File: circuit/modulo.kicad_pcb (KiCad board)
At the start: 2 copper layers, 302 x 135 mm, 201 parts, among them J1 JACK_MONO, J10 HOLE, J11 HOLE, J12 HOLE, J13 HOLE, J14 HOLE, J15 HOLE, J17 HOLE, J18 HOLE, J19 HOLE, J2 Barrel_Jack_Switch, J24 HOLE, J25 HOLE, J26 HOLE, J27 HOLE, J3 HOLE, J4 HOLE, J5 HOLE, J6 HOLE, J7 HOLE, J8 HOLE, J9 HOLE, Q1 MMBFJ201, Q2 BC547, Q3 BC557, Q4 BC547, Q5 BC557, SW1 OFF/ON, SW2 ROT_SW, SW3 Idss/Vp, SW4 disc/TLE2426, SW5 disc/TLE2426, U1 TLE2426, U10 AVR-ISP6, U11 74164, U12 TPA3136D2, U13 74164, U14 modulo-bus, U15 modulo-bus, U16 modulo-bus, U17 TLE2426, U18 DBG_UART, U19 TPS560430, U2 NE5532, U3 FV-1, U4 NE5532, U5 24LC32A, U6 modulo-bus, U7 LM1117, U8 modulo-bus, U9 ATMEGA8, Y1 32768Hz, Y2 8MHz

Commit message: added pot and rotenc datasheets; cosmetics
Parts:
- moved J1 0.32 mm to (11.7, 17.8)
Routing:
- net +12V: track 508.1 -> 503.5 mm
- net Net-(RV6-Pad2): track 55.2 -> 54.1 mm
- net /pre amp/jfet_g: track 49.4 -> 50.1 mm

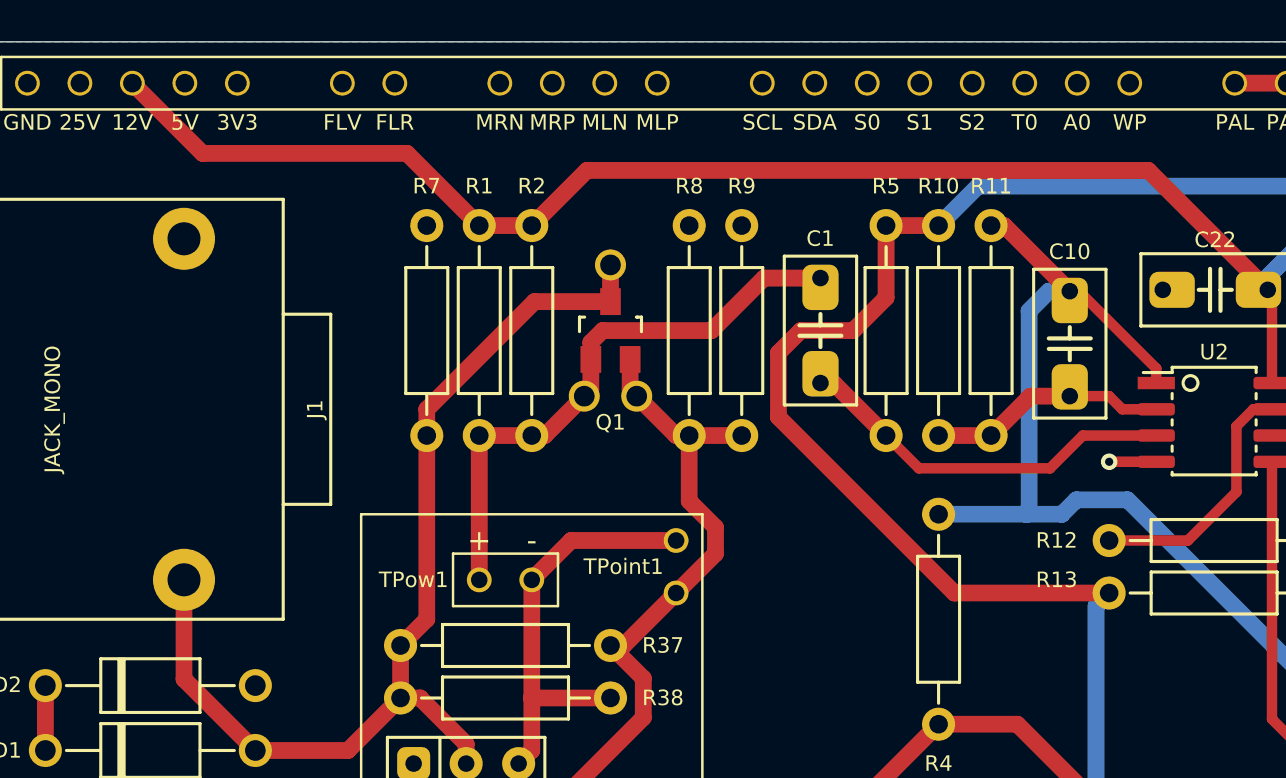
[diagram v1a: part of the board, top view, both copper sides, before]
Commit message: ccw/cw on pots; new values of the tone stack
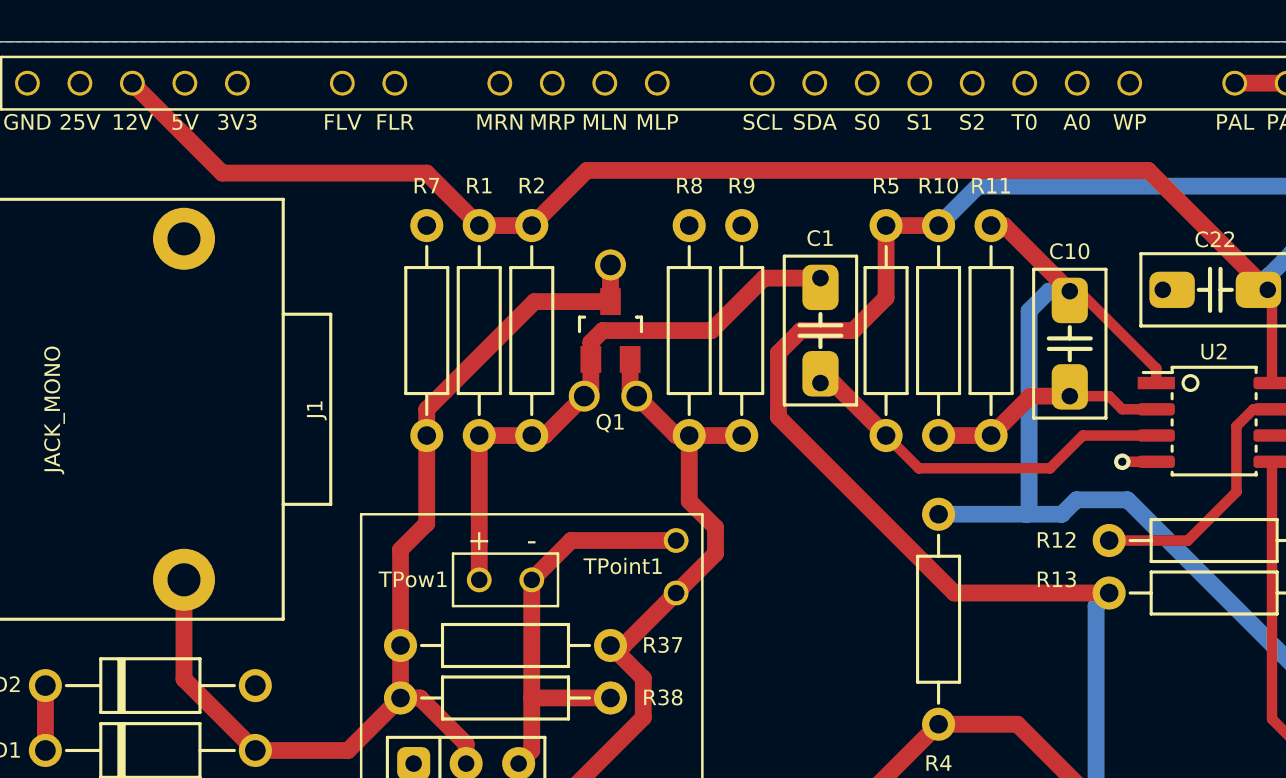
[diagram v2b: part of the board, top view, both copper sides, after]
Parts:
- C2: value 250pF -> 680pF
- C8: value 100nF -> 250nF
- RV1, RV2: value 250K -> A100K
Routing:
- net GND: track 108.9 -> 108.3 mm
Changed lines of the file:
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@@
     (thickness 1.6)
     (drawings 50)
-    (tracks 1037)
+    (tracks 1038)
     (zones 0)
     (modules 201)
@@
   )
   (setup
-    (last_trace_width 0.8128)
+    (last_trace_width 0.2032)
     (user_trace_width 0.254)
     (user_trace_width 0.3048)
@@
       (effects (font (size 0.75 0.75) (thickness 0.15)))
     )
-    (fp_text value 100nF (at -1.016 -0.254) (layer F.Fab) hide
+    (fp_text value 250nF (at -1.016 -0.254) (layer F.Fab) hide
       (effects (font (size 0.127 0.127) (thickness 0.001)))
     )
@@
       (effects (font (size 0.75 0.75) (thickness 0.15)))
     )
-    (fp_text value 250pF (at -1.016 -0.254) (layer F.Fab) hide
+    (fp_text value 680pF (at -1.016 -0.254) (layer F.Fab) hide
       (effects (font (size 0.127 0.127) (thickness 0.001)))
     )
@@
       (effects (font (size 0.75 0.75) (thickness 0.15)))
     )
-    (fp_text value 250K (at 0 -0.5) (layer F.Fab)
+    (fp_text value A100K (at 0 -0.5) (layer F.Fab)
       (effects (font (size 0.03 0.03) (thickness 0.0075)))
     )
@@
       (effects (font (size 0.75 0.75) (thickness 0.15)))
     )
-    (fp_text value 250K (at 0 -0.5) (layer F.Fab)
+    (fp_text value A100K (at 0 -0.5) (layer F.Fab)
       (effects (font (size 0.03 0.03) (thickness 0.0075)))
     )
@@
   (via (at 38.735 105.41) (size 0.8) (drill 0.4) (layers F.Cu B.Cu) (net 3))
   (segment (start 40.38 105.41) (end 38.735 105.41) (width 0.508) (layer F.Cu) (net 3))
-  (via (at 62.865 20.32) (size 0.8) (drill 0.4) (layers F.Cu B.Cu) (net 3))
-  (segment (start 65.145 20.32) (end 62.865 20.32) (width 0.508) (layer F.Cu) (net 3))
+  (segment (start 65.145 20.32) (end 63.5 20.32) (width 0.508) (layer F.Cu) (net 3))
+  (via (at 63.5 20.32) (size 0.8) (drill 0.4) (layers F.Cu B.Cu) (net 3))
   (segment (start 257.445 24.765) (end 257.6 24.61) (width 0.508) (layer F.Cu) (net 4))
   (segment (start 253.085 24.765) (end 257.445 24.765) (width 0.508) (layer F.Cu) (net 4))
@@
   (segment (start 70.54 11.37) (end 71.75 10.16) (width 0.8128) (layer B.Cu) (net 57))
   (segment (start 32.385 8.89) (end 34.925 8.89) (width 0.8128) (layer F.Cu) (net 57))
-  (segment (start 15.6 2) (end 18.9975 5.3975) (width 0.8128) (layer F.Cu) (net 57))
-  (segment (start 28.8925 5.3975) (end 32.385 8.89) (width 0.8128) (layer F.Cu) (net 57))
-  (segment (start 18.9975 5.3975) (end 28.8925 5.3975) (width 0.8128) (layer F.Cu) (net 57))
   (segment (start 34.925 8.89) (end 37.592 6.223) (width 0.8128) (layer F.Cu) (net 57))
   (segment (start 64.763 6.223) (end 70.54 12) (width 0.8128) (layer F.Cu) (net 57))
@@
   (segment (start 120.65 38.0365) (end 120.65 27.94) (width 0.8128) (layer F.Cu) (net 57))
   (segment (start 119.22125 39.46525) (end 120.65 38.0365) (width 0.8128) (layer F.Cu) (net 57))
+  (segment (start 29.845 6.35) (end 32.385 8.89) (width 0.8128) (layer F.Cu) (net 57))
+  (segment (start 15.6 2) (end 19.95 6.35) (width 0.8128) (layer F.Cu) (net 57))
+  (segment (start 19.95 6.35) (end 29.845 6.35) (width 0.8128) (layer F.Cu) (net 57))
   (segment (start 65.145 16.51) (end 65.145 15.8055) (width 0.508) (layer F.Cu) (net 58))
   (segment (start 61.4045 12.065) (end 60.96 12.065) (width 0.508) (layer F.Cu) (net 58))
@@
   (segment (start 38.735 12.57) (end 35.055 12.57) (width 0.8128) (layer F.Cu) (net 60))
   (segment (start 35.055 12.57) (end 29.845 17.78) (width 0.8128) (layer F.Cu) (net 60))
-  (segment (start 29.845 27.94) (end 28.575 29.21) (width 0.8128) (layer F.Cu) (net 60))
-  (segment (start 29.845 19.05) (end 29.845 27.94) (width 0.8128) (layer F.Cu) (net 60))
   (segment (start 28.575 29.21) (end 28.575 31.75) (width 0.8128) (layer F.Cu) (net 60))
   (segment (start 26.035 34.29) (end 28.575 31.75) (width 0.8128) (layer F.Cu) (net 60))
@@
   (segment (start 18.0975 30.837501) (end 21.549999 34.29) (width 0.8128) (layer F.Cu) (net 60))
   (segment (start 18.0975 26.03) (end 18.0975 30.837501) (width 0.8128) (layer F.Cu) (net 60))
+  (segment (start 28.575 24.5745) (end 28.575 29.21) (width 0.8128) (layer F.Cu) (net 60))
+  (segment (start 29.845 19.05) (end 29.845 23.3045) (width 0.8128) (layer F.Cu) (net 60))
+  (segment (start 29.845 23.3045) (end 28.575 24.5745) (width 0.8128) (layer F.Cu) (net 60))
   (segment (start 37.785 16.825) (end 37.465 17.145) (width 0.8128) (layer F.Cu) (net 61))
   (segment (start 37.785 15.37) (end 37.785 16.825) (width 0.8128) (layer F.Cu) (net 61))

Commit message: front copper plant; pot descriptions
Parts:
- moved C12 5.43 mm to (48.9, 34.3), turned to 180 degrees
- moved C2 5.08 mm to (74.9, 34.3)
- moved C8 5.08 mm to (62.2, 34.3)
- moved Q2 5.08 mm to (94.6, 33.0)
- moved Q3 5.08 mm to (87.0, 33.0)
- moved D4 4.45 mm to (94.6, 24.8)
- moved D5 4.45 mm to (87.0, 24.8)
- moved R15 4.45 mm to (97.2, 24.8)
- moved R22 4.45 mm to (92.1, 24.8)
- moved R25 4.45 mm to (89.5, 24.8)
- moved R27 4.45 mm to (84.5, 24.8)
- moved C16 3.17 mm to (94.6, 14.0)
- moved C20 3.17 mm to (87.0, 14.0)
- moved U1 1.27 mm to (90.8, 8.26)
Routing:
- net Net-(C12-Pad1): track 21.8 -> 15.0 mm
- net Net-(C12-Pad2): track 55.6 -> 50.2 mm
- net Net-(C8-Pad1): track 52.5 -> 57.6 mm
- net Net-(C10-Pad1): track 54.0 -> 49.0 mm
- net /pre amp/vgnd_disc: track 36.8 -> 32.4 mm
- net +12V: track 503.5 -> 499.7 mm
- net /power and MCU/SCL: track 21.0 -> 23.2 mm
- net Net-(C2-Pad1): track 13.5 -> 15.6 mm
- net Net-(RN2-Pad7): track 26.9 -> 28.6 mm
- net /power and MCU/SDA: track 20.3 -> 21.7 mm
- net /pre amp/vgnd_tle: track 6.35 -> 5.08 mm
- net Net-(C31-Pad1): track 21.9 -> 22.6 mm
- net Net-(Q3-Pad3): track 3.81 -> 3.18 mm
- net Net-(Q2-Pad3): track 3.81 -> 3.18 mm
- net Net-(D5-Pad1): track 7.62 -> 6.99 mm
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- added copper zone on F.Cu, net GND
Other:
- board text added: "bass"
- board text added: "master"
- board text added: "mid"
- board text added: "param 1"
- board text added: "param 2"
- board text added: "param 3"
- board text added: "program"
- board text added: "treble"
- board text added: "wet/dry"

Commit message: this one goes to fab
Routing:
- net +3V3: track 334.3 -> 339.7 mm
- net Net-(RV1-Pad2): track 35.2 -> 32.0 mm
- net Net-(C8-Pad1): track 57.6 -> 58.1 mm
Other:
- board text added: "2020/jun/21"
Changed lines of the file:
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@@
   (general
     (thickness 1.6)
-    (drawings 59)
-    (tracks 1072)
+    (drawings 64)
+    (tracks 1071)
     (zones 0)
     (modules 201)
@@
   )
   (setup
-    (last_trace_width 0.4064)
+    (last_trace_width 0.2032)
     (user_trace_width 0.254)
     (user_trace_width 0.3048)
@@
     )
   )
+  (gr_text 2020/jun/21 (at 179.5145 116.3955) (layer B.SilkS)
+    (effects (font (size 2 2) (thickness 0.4)) (justify mirror))
+  )
+  (gr_text 2020/jun/21 (at 289.56 36.449) (layer B.SilkS)
+    (effects (font (size 2 2) (thickness 0.4)) (justify mirror))
+  )
+  (gr_text 2020/jun/21 (at 85.0265 96.4565) (layer B.SilkS)
+    (effects (font (size 2 2) (thickness 0.4)) (justify mirror))
+  )
+  (gr_text 2020/jun/21 (at 172.6565 7.747) (layer B.SilkS)
+    (effects (font (size 2 2) (thickness 0.4)) (justify mirror))
+  )
+  (gr_text 2020/jun/21 (at 15.113 15.8115) (layer B.SilkS)
+    (effects (font (size 2 2) (thickness 0.4)) (justify mirror))
+  )
   (gr_text "param 3" (at 285.115 41.91) (layer F.SilkS)
     (effects (font (size 2 2) (thickness 0.3)))
@@
   (segment (start 51.435 34.29) (end 53.34 34.29) (width 0.8128) (layer F.Cu) (net 6))
   (segment (start 35.56 44.45) (end 38.06 44.45) (width 0.8128) (layer F.Cu) (net 7))
-  (segment (start 38.5045 44.0055) (end 38.06 44.45) (width 0.8128) (layer F.Cu) (net 7))
-  (segment (start 52.54625 44.0055) (end 38.5045 44.0055) (width 0.8128) (layer F.Cu) (net 7))
-  (segment (start 59.69 39.37) (end 57.18175 39.37) (width 0.8128) (layer F.Cu) (net 7))
-  (segment (start 57.18175 39.37) (end 52.54625 44.0055) (width 0.8128) (layer F.Cu) (net 7))
   (segment (start 59.69 39.37) (end 61.595 39.37) (width 0.8128) (layer F.Cu) (net 7))
   (segment (start 66.675 44.45) (end 83.86 44.45) (width 0.8128) (layer F.Cu) (net 7))
   (segment (start 61.595 39.37) (end 66.675 44.45) (width 0.8128) (layer F.Cu) (net 7))
   (segment (start 59.69 34.29) (end 59.69 39.37) (width 0.8128) (layer F.Cu) (net 7))
+  (segment (start 55.499 44.45) (end 38.06 44.45) (width 0.8128) (layer F.Cu) (net 7))
+  (segment (start 59.69 39.37) (end 59.69 40.259) (width 0.8128) (layer F.Cu) (net 7))
+  (segment (start 59.69 40.259) (end 55.499 44.45) (width 0.8128) (layer F.Cu) (net 7))
   (segment (start 54.61 19.05) (end 57.15 19.05) (width 0.8128) (layer F.Cu) (net 8))
   (segment (start 59.055 17.145) (end 57.15 19.05) (width 0.8128) (layer F.Cu) (net 8))
@@
   (segment (start 251.2695 28.575) (end 253.085 28.575) (width 0.508) (layer F.Cu) (net 10))
   (segment (start 250.15 29.6945) (end 251.2695 28.575) (width 0.508) (layer F.Cu) (net 10))
-  (segment (start 224.75 43.394) (end 224.75 44.45) (width 0.8128) (layer F.Cu) (net 10))
-  (segment (start 216.916 35.56) (end 224.75 43.394) (width 0.8128) (layer F.Cu) (net 10))
-  (segment (start 228.715 28.575) (end 228.715 29.282106) (width 0.8128) (layer F.Cu) (net 10))
-  (segment (start 226.183606 31.8135) (end 218.2495 31.8135) (width 0.8128) (layer F.Cu) (net 10))
-  (segment (start 218.2495 31.8135) (end 216.916 33.147) (width 0.8128) (layer F.Cu) (net 10))
-  (segment (start 216.916 33.147) (end 216.916 35.56) (width 0.8128) (layer F.Cu) (net 10))
-  (segment (start 229.87 33.655) (end 227.137803 30.922803) (width 0.8128) (layer F.Cu) (net 10))
-  (segment (start 228.715 29.282106) (end 227.137803 30.859303) (width 0.8128) (layer F.Cu) (net 10))
-  (segment (start 227.137803 30.922803) (end 227.137803 30.859303) (width 0.8128) (layer F.Cu) (net 10))
-  (segment (start 227.137803 30.859303) (end 226.183606 31.8135) (width 0.8128) (layer F.Cu) (net 10))
   (segment (start 283.7415 44.45) (end 286.266 46.9745) (width 0.8128) (layer F.Cu) (net 10))
   (segment (start 275.55 44.45) (end 283.7415 44.45) (width 0.8128) (layer F.Cu) (net 10))
@@
   (segment (start 175.475889 115.531889) (end 172.2755 112.3315) (width 0.4064) (layer F.Cu) (net 10))
   (segment (start 172.2755 112.3315) (end 165.227 112.3315) (width 0.4064) (layer F.Cu) (net 10))
+  (segment (start 228.715 32.5) (end 229.87 33.655) (width 0.8128) (layer F.Cu) (net 10))
+  (segment (start 228.715 30.214) (end 228.715 32.5) (width 0.8128) (layer F.Cu) (net 10))
+  (segment (start 228.715 28.575) (end 228.715 30.214) (width 0.8128) (layer F.Cu) (net 10))
+  (segment (start 224.75 43.3305) (end 224.75 44.45) (width 0.8128) (layer F.Cu) (net 10))
+  (segment (start 222.0595 40.64) (end 224.75 43.3305) (width 0.8128) (layer F.Cu) (net 10))
+  (segment (start 217.3725 30.214) (end 215.265 32.3215) (width 0.8128) (layer F.Cu) (net 10))
+  (segment (start 228.715 30.214) (end 217.3725 30.214) (width 0.8128) (layer F.Cu) (net 10))
+  (segment (start 215.265 32.3215) (end 215.265 37.4015) (width 0.8128) (layer F.Cu) (net 10))
+  (segment (start 215.265 37.4015) (end 218.5035 40.64) (width 0.8128) (layer F.Cu) (net 10))
+  (segment (start 218.5035 40.64) (end 222.0595 40.64) (width 0.8128) (layer F.Cu) (net 10))
   (segment (start 27.94 100.33) (end 27.94 102.87) (width 0.8128) (layer F.Cu) (net 11))
   (segment (start 64.77 99.06) (end 64.77 101.6) (width 0.8128) (layer F.Cu) (net 12))
@@
   (segment (start 253.085 23.495) (end 255.215 23.495) (width 0.508) (layer F.Cu) (net 53))
   (segment (start 86.36 44.069) (end 86.36 44.45) (width 0.508) (layer F.Cu) (net 54))
-  (segment (start 84.963 42.672) (end 86.36 44.069) (width 0.508) (layer F.Cu) (net 54))
   (segment (start 70.745 28.2) (end 74.93 32.385) (width 0.508) (layer F.Cu) (net 54))
-  (segment (start 74.93 32.385) (end 74.93 40.5765) (width 0.508) (layer F.Cu) (net 54))
   (segment (start 70.745 20.32) (end 70.745 28.2) (width 0.508) (layer F.Cu) (net 54))
-  (segment (start 74.93 40.5765) (end 77.0255 42.672) (width 0.508) (layer F.Cu) (net 54))
-  (segment (start 77.0255 42.672) (end 84.963 42.672) (width 0.508) (layer F.Cu) (net 54))
+  (segment (start 74.93 32.385) (end 74.93 35.1155) (width 0.508) (layer F.Cu) (net 54))
+  (segment (start 74.93 35.1155) (end 75.946 36.1315) (width 0.508) (layer F.Cu) (net 54))
+  (segment (start 78.4225 36.1315) (end 86.36 44.069) (width 0.508) (layer F.Cu) (net 54))
+  (segment (start 75.946 36.1315) (end 78.4225 36.1315) (width 0.508) (layer F.Cu) (net 54))
   (segment (start 273.05 45.4025) (end 273.05 44.45) (width 0.508) (layer F.Cu) (net 55))
   (segment (start 271.2085 47.244) (end 273.05 45.4025) (width 0.508) (layer F.Cu) (net 55))
@@
   (segment (start 251.523496 18.415) (end 249.809 16.700504) (width 0.508) (layer F.Cu) (net 94))
   (segment (start 253.085 18.415) (end 251.523496 18.415) (width 0.508) (layer F.Cu) (net 94))
-  (segment (start 246.4435 13.335004) (end 249.809 16.700504) (width 0.8128) (layer B.Cu) (net 94))
-  (segment (start 246.4435 11.3665) (end 246.4435 13.335004) (width 0.8128) (layer B.Cu) (net 94))
+  (segment (start 247.5865 12.5095) (end 247.5865 14.478004) (width 0.8128) (layer B.Cu) (net 94))
   (segment (start 244.475 10.16) (end 245.237 10.16) (width 0.8128) (layer B.Cu) (net 94))
-  (segment (start 245.237 10.16) (end 246.4435 11.3665) (width 0.8128) (layer B.Cu) (net 94))
+  (segment (start 247.5865 14.478004) (end 249.809 16.700504) (width 0.8128) (layer B.Cu) (net 94))
+  (segment (start 245.237 10.16) (end 247.5865 12.5095) (width 0.8128) (layer B.Cu) (net 94))
   (segment (start 69.215 99.06) (end 69.215 101.6) (width 0.8128) (layer F.Cu) (net 95))
   (segment (start 54.015 129.5) (end 65.405 118.11) (width 0.8128) (layer F.Cu) (net 96))
@@
   (segment (start 153.27 101.2) (end 153.035 100.965) (width 0.4064) (layer F.Cu) (net 116))
   (segment (start 153.27 104.72) (end 153.27 101.2) (width 0.4064) (layer F.Cu) (net 116))
-  (segment (start 159.766 100.965) (end 168.402 109.601) (width 0.4064) (layer B.Cu) (net 116))
   (via (at 168.402 109.601) (size 0.8) (drill 0.4) (layers F.Cu B.Cu) (net 116))
-  (segment (start 153.035 100.965) (end 159.766 100.965) (width 0.4064) (layer B.Cu) (net 116))
   (segment (start 175.895 114.7445) (end 172.593 111.4425) (width 0.4064) (layer F.Cu) (net 116))
   (segment (start 172.593 111.4425) (end 170.2435 111.4425) (width 0.4064) (layer F.Cu) (net 116))
@@
   (segment (start 198.882 121.285) (end 199.517 120.65) (width 0.4064) (layer F.Cu) (net 116))
   (segment (start 199.517 120.65) (end 199.517 116.84) (width 0.4064) (layer F.Cu) (net 116))
+  (segment (start 159.766 100.965) (end 168.402 109.601) (width 0.8128) (layer B.Cu) (net 116))
+  (segment (start 153.035 100.965) (end 159.766 100.965) (width 0.8128) (layer B.Cu) (net 116))
   (segment (start 182.285 127.8655) (end 170.294278 115.874778) (width 0.4064) (layer F.Cu) (net 117))
   (segment (start 182.285 129.54) (end 182.285 127.8655) (width 0.4064) (layer F.Cu) (net 117))
